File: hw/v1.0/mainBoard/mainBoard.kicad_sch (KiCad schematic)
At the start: 64 parts, among them J15 U.FL, J4 PROGRAMMER, J6 EN_3V3_PROGRAMMER, Q1 MMBT3904, Q14 AO3401A, Q15 2N7002, Q2 MMBT3904, SW1 PWR_ON, SW2 PWR_OFF, SW3 RESET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

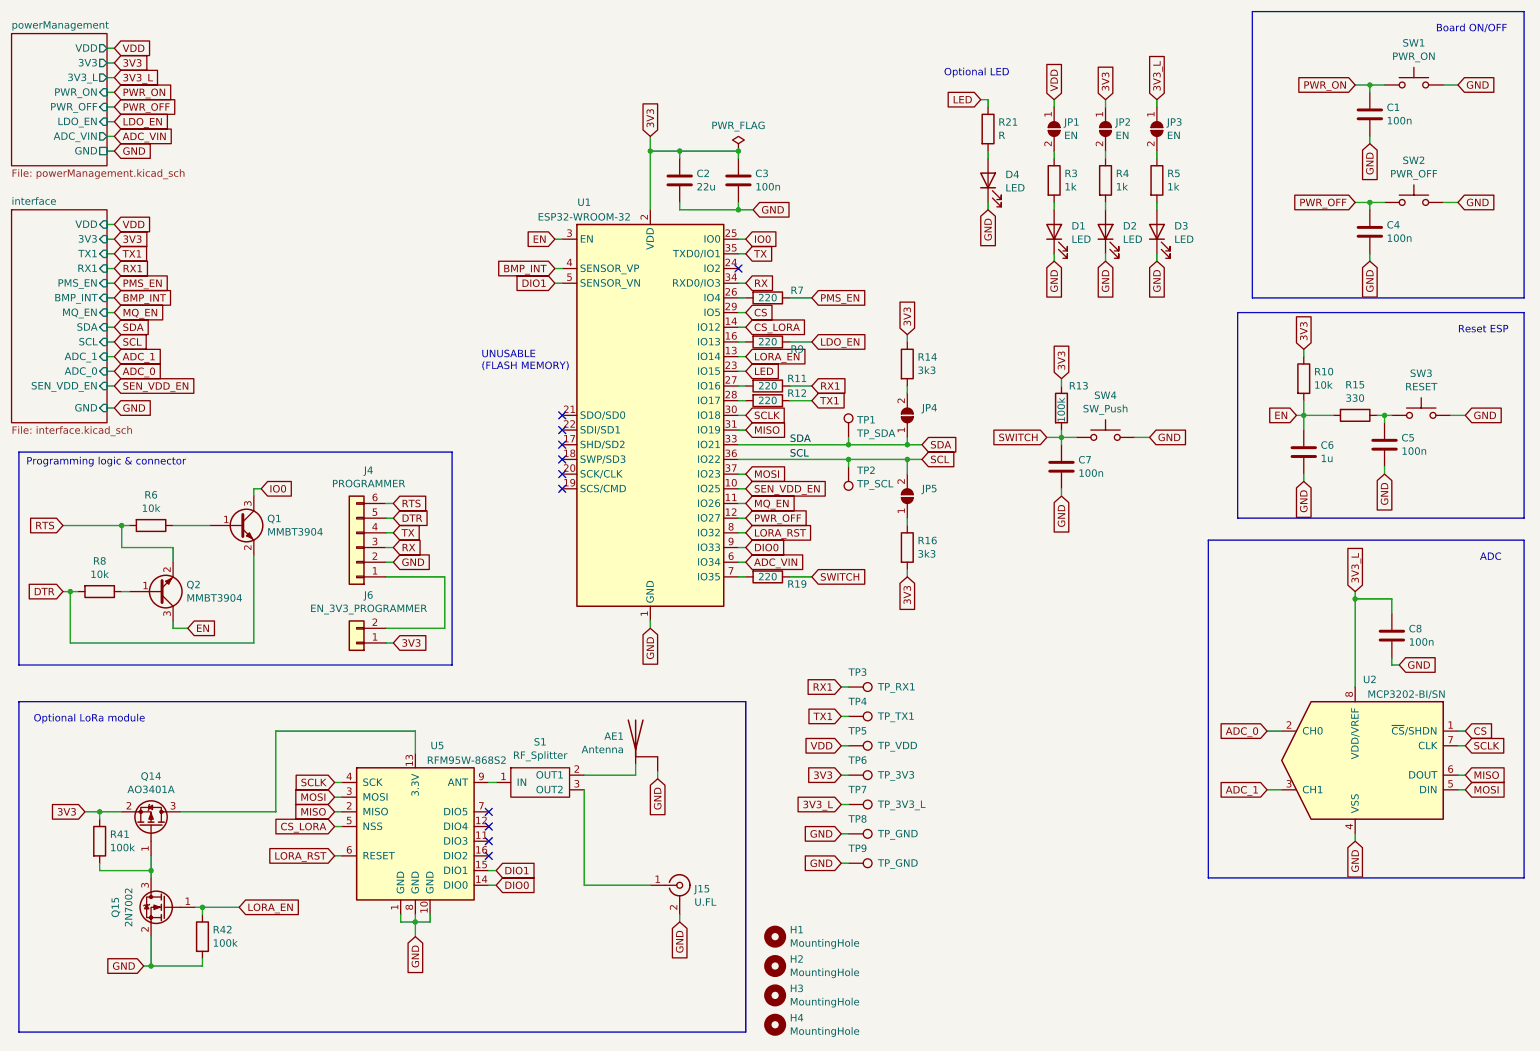
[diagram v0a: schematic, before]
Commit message: Start routing PCB
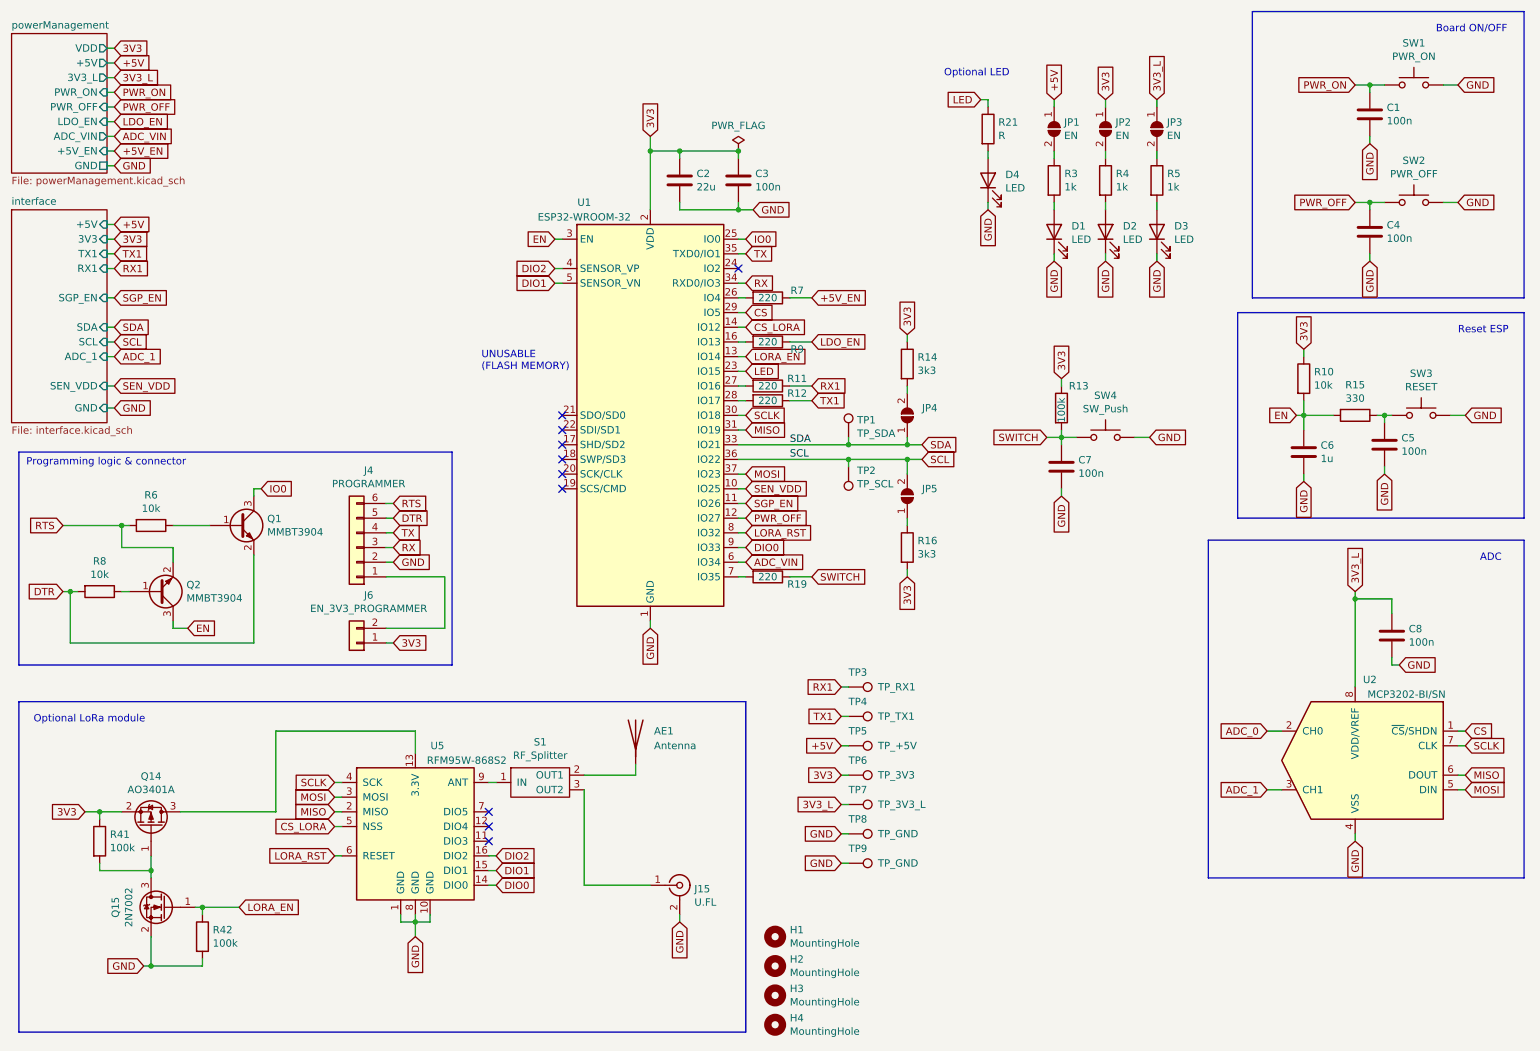
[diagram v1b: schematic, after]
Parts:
- AE1: footprint RF_Antenna:Texas_SWRA416_868MHz_915MHz -> mainBoard:ANT-868-CHP-T; TME (none) -> ANT-868-CHP-T
- C1, C3, C4, C5, C7, C8: footprint Capacitor_SMD:C_0402_1005Metric -> Capacitor_SMD:C_0603_1608Metric
- C6: footprint Capacitor_SMD:C_0402_1005Metric -> Capacitor_SMD:C_0805_2012Metric
- R10, R11, R12, R13, R14, R15, R16, R19, R3, R4, R41, R42, R5, R6, R7, R8, R9: footprint Resistor_SMD:R_0402_1005Metric -> Resistor_SMD:R_0805_2012Metric
- S1: footprint iotAirMonitoring:RF_Splitter -> mainBoard:RF_Splitter
- TP5: value TP_VDD -> TP_+5V
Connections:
- net BMP_INT is gone; now on net DIO2: U1.4 (SENSOR_VP)
- net GND: no longer AE1.2 (GND), AE1.3 (GND)
- net DIO2: now reaches U5.16 (DIO2)
- net MQ_EN renamed SGP_EN
- net PMS_EN renamed +5V_EN
- net SEN_VDD_EN renamed SEN_VDD
- net VDD renamed +5V
- no-connect marks 11 -> 10
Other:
- sheet interface ports: added +5V, SEN_VDD, SGP_EN; removed ADC_0, BMP_INT, MQ_EN, PMS_EN, SEN_VDD_EN, VDD
- sheet powerManagement ports: added +5V, +5V_EN; removed 3V3

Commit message: Start routing mainBoard
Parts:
- R21: footprint Resistor_SMD:R_0805_2012Metric_Pad1.20x1.40mm_HandSolder -> Resistor_SMD:R_0805_2012Metric
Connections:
- net SDA: now also JP4.2 (B); no longer JP4.1 (A)
- net at R14.2: now also JP4.1 (A); no longer JP4.2 (B)
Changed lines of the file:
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@@
       (effects (font (size 1.27 1.27)) (justify left))
     )
-    (property "Footprint" "Resistor_SMD:R_0805_2012Metric_Pad1.20x1.40mm_HandSolder" (id 2) (at 186.182 34.29 90)
+    (property "Footprint" "Resistor_SMD:R_0805_2012Metric" (id 2) (at 186.182 34.29 90)
       (effects (font (size 1.27 1.27)) hide)
     )
@@
     (pin "2")
   )
-  (symbol (lib_id "Jumper:SolderJumper_2_Open") (at 173.99 83.82 90) (unit 1)
+  (symbol (lib_id "Jumper:SolderJumper_2_Open") (at 173.99 83.82 90) (mirror x) (unit 1)
     (in_bom yes) (on_board yes) (fields_autoplaced)
     (property "Reference" "JP4" (id 0) (at 176.53 82.5499 90)
@@
     )
     (path "/00000000-0000-0000-0000-000061a0488a"
-      (reference "R21") (unit 1) (value "R") (footprint "Resistor_SMD:R_0805_2012Metric_Pad1.20x1.40mm_HandSolder")
+      (reference "R21") (unit 1) (value "R") (footprint "Resistor_SMD:R_0805_2012Metric")
     )
     (path "/00000000-0000-0000-0000-000061d2d467/5febcca7-fd23-4dc0-87e2-44a1a99b60ba"
